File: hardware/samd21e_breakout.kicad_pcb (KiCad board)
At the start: 2 copper layers, 35.7 x 21.6 mm, 12 parts, among them J1 USB_B_Micro, J2 Conn_01x26_Male, J3 Conn_01x08_Male, SW1 SW_Push, U1 AP2112K-3.3, U2 ATSAMD21E18A, Y1 32.768 kHz

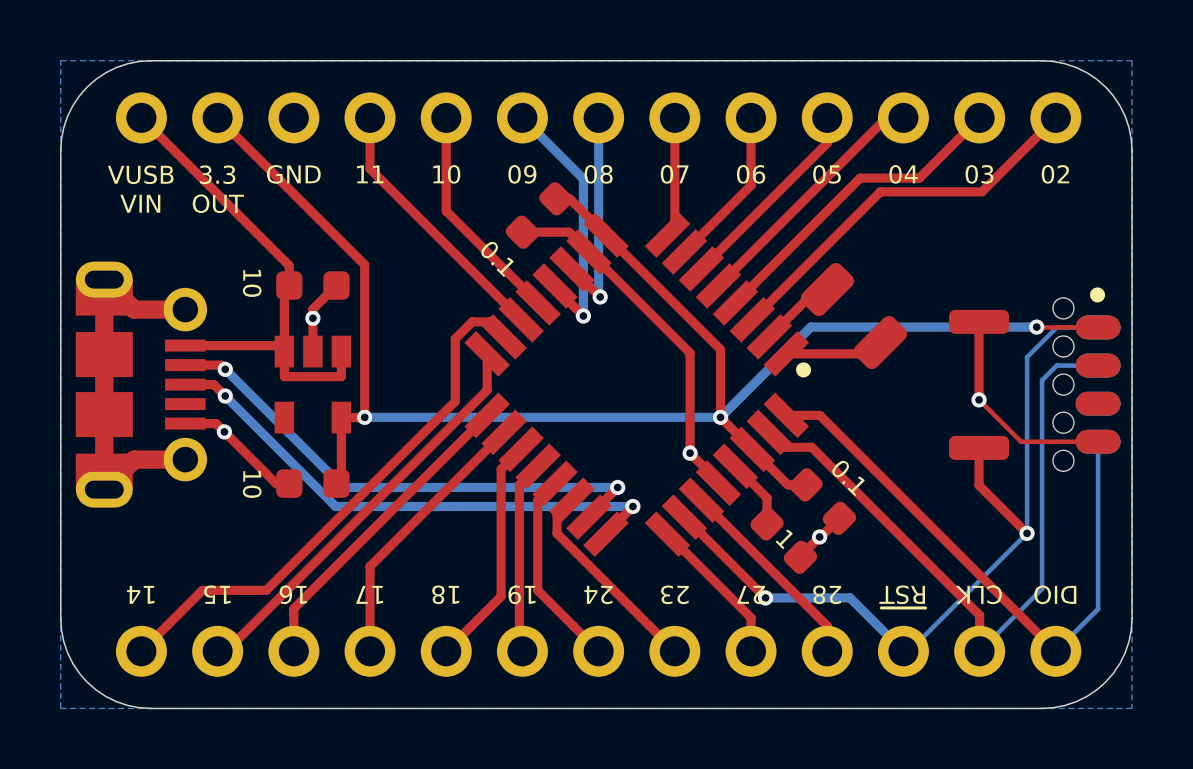
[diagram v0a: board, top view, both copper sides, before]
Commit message: added load capacitors to schematic and pcb
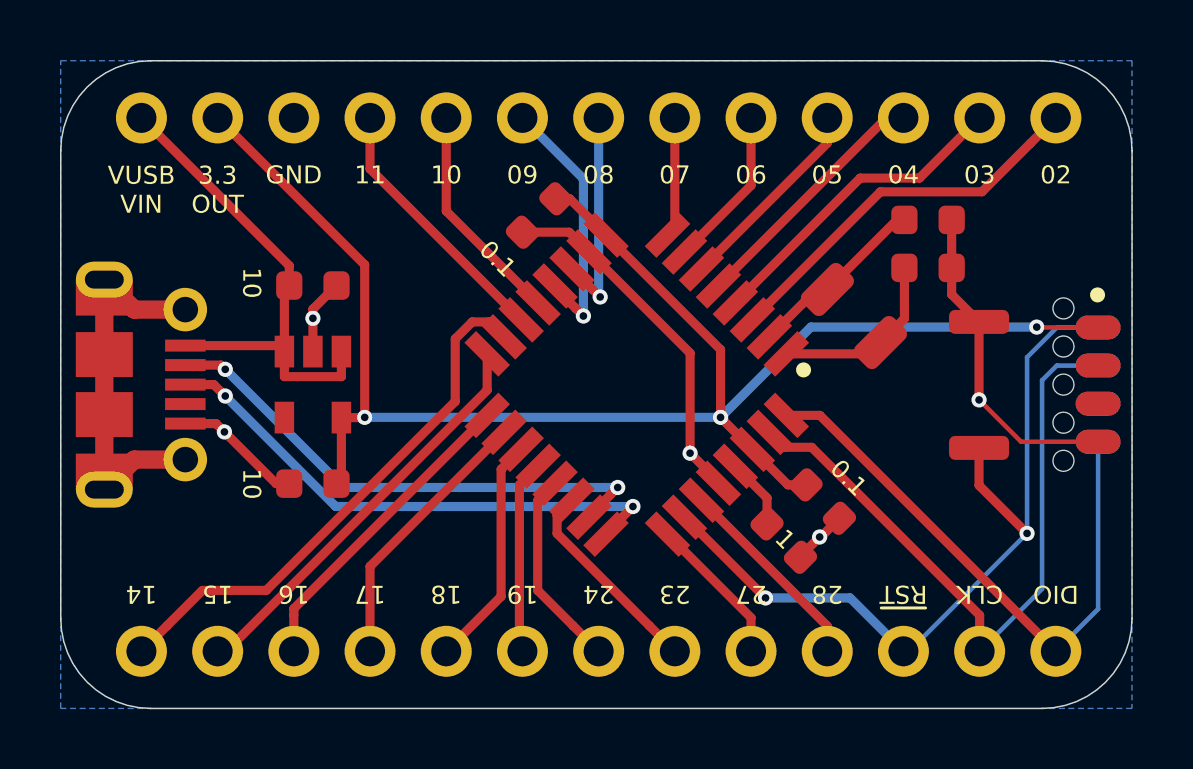
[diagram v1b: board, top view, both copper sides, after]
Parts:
- added C6: 10p, samd21e_breakout:C_0603_NoSilk, F.Cu at (45.9, 23.9)
- added C7: 10p, samd21e_breakout:C_0603_NoSilk, F.Cu at (45.9, 22.3)
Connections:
- net Net-(U2-Pad1) renamed /XIN32
- net Net-(U2-Pad2) renamed /XOUT32
- J1 pad 4: (no net) -> Net-(J1-Pad4)
- J3 pad 2: (no net) -> Net-(J3-Pad2)
- J3 pad 3: (no net) -> Net-(J3-Pad3)
- J3 pad 6: (no net) -> Net-(J3-Pad6)
- U1 pad 4: (no net) -> Net-(U1-Pad4)
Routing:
- net GND: track 27.8 -> 31.6 mm
- net /XOUT32: track 2.59 -> 6.12 mm
- net /XIN32: track 3.29 -> 6.11 mm

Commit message: Long overdue update to readme, upgrade to KiCad 6
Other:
- net class Default removed
- board text added: "~{RST}"
- board text removed: "~RST"
